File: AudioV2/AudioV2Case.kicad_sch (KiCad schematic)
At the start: 0 parts

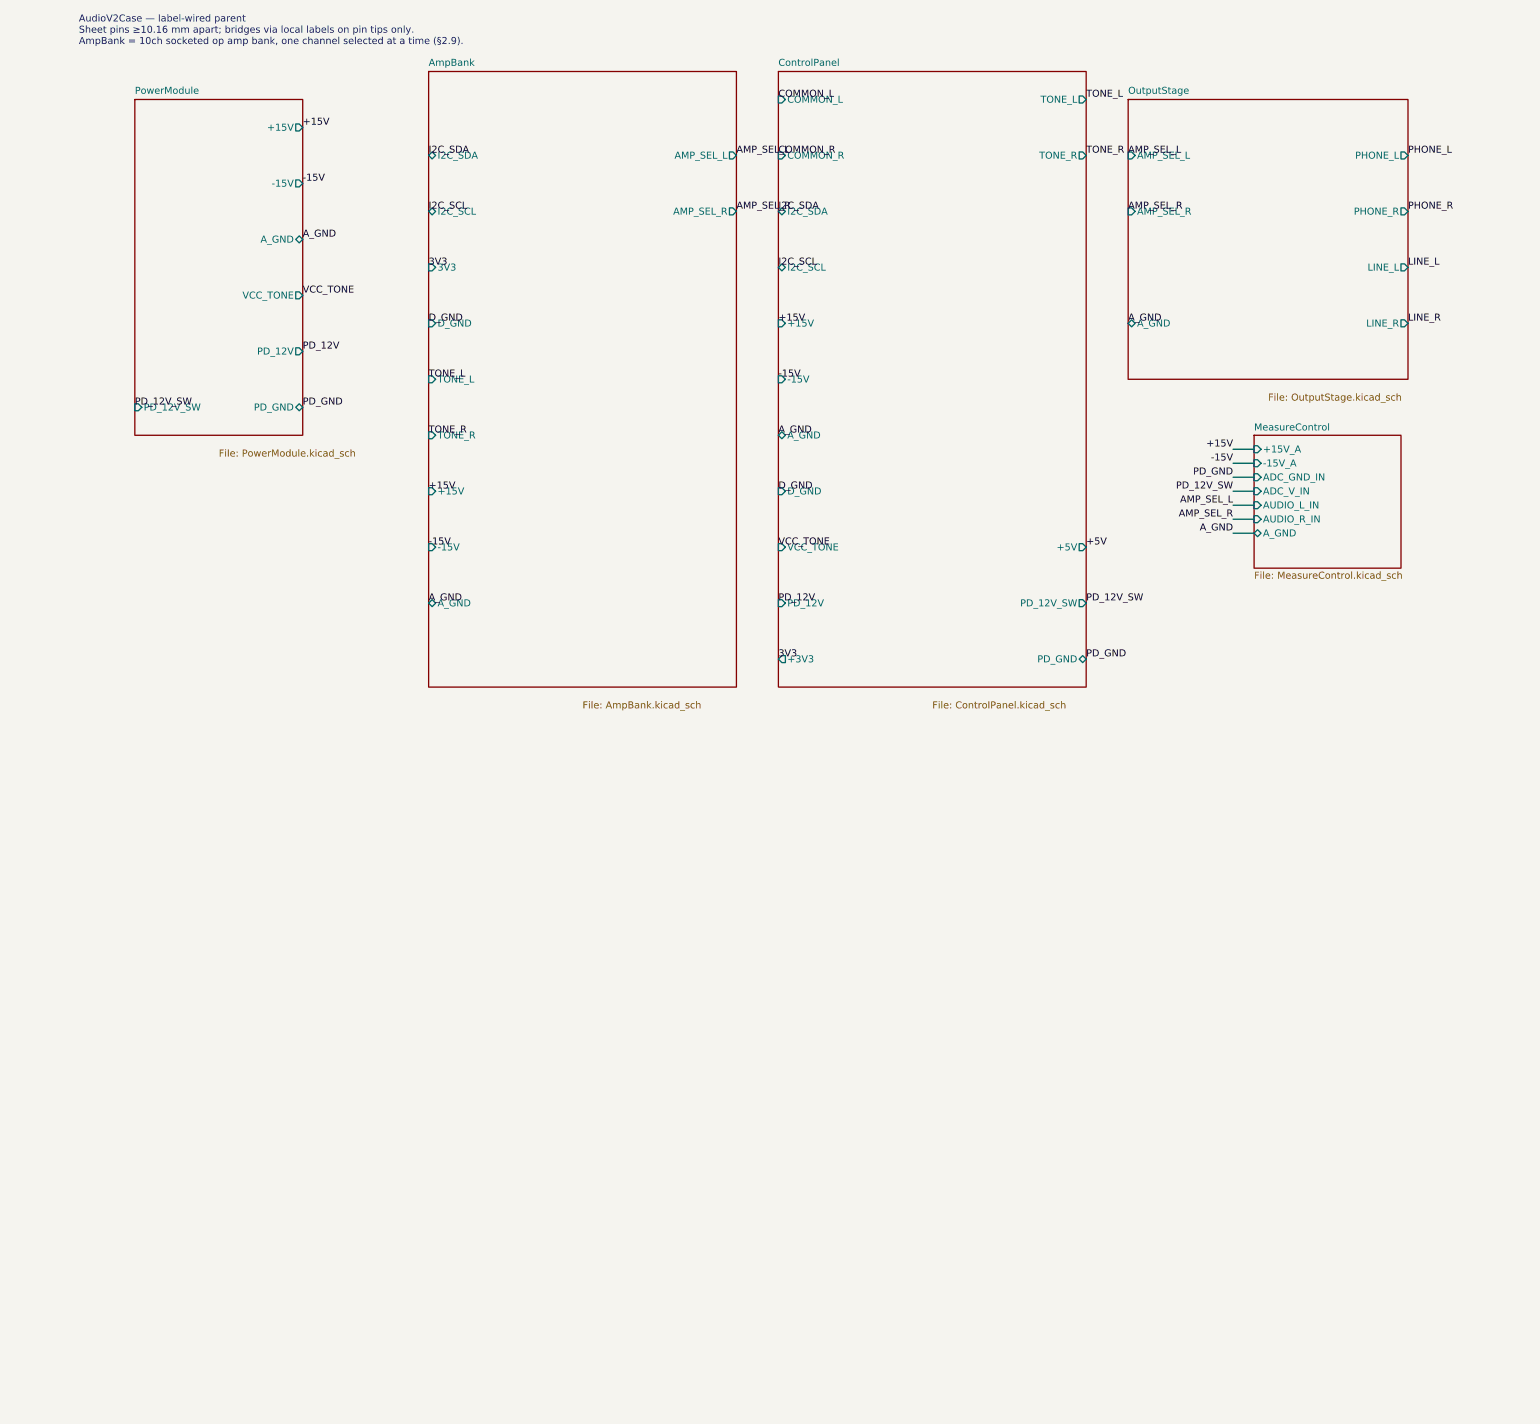
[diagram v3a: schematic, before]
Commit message: AudioV2: 母板 v0 を生成コードで組み立て、PowerModule と OutputStage を統合
確定している部分だけの骨格。PT2314 の移設と ControlPanel の解体は未決なので
触っていない（未決のまま足すと検証できない）。娘基板スロットは次のステップ。

    母板 v0 = PowerModule の全要素 ＋ OutputStage の全要素（+111.76mm 平行移動）

旧シートは sch_import で **KiCad が書いた S式のまま** 読むので、
**手描きの配線 92 本とジャンクション 33 個がそのまま母板へ移った**。
書き起こし直していたら失われていた部分。

統合の処理:
- 重複する階層ラベル A_GND（両シートが親経由で繋がっていた）を1本に。
  OutputStage 側はローカルラベルへ落として結線を保つ
- 各シンボルの instances パスを母板のシート UUID へ付け替え
- lib_symbols を名前で重複排除して統合
- 親から PowerModule / OutputStage のシートと、そのピン上にあった
  ラベル 14 個を外し、母板シート（階層ピン 13 本）＋ラベル 13 個に置換

新規ツール:
- build_motherboard.py — 母板の生成コード。再実行は冪等で、
  **UUID も決定的**（2回流してバイト一致を確認）。§2.8 の
  「再生成すると 348 行の uuid が毎回変わる」問題を持ち込まないため
- netlist_partition.py — ネットリストを「ピン集合の集合」で比較する。
  シート統合ではネット**名**は変わるが**分割**は変わってはいけない。
  sch_drift.py はワイヤを見ないので統合の検証には使えない

検証:
- ネットリストの分割が **310 ネットで完全一致**。名前だけ 4 件が
  /OutputStage/* → /MotherBoard/* に変化（シート内ネットなので当然）
- **ERC 60 件で前後同一**（内訳も同じ）
- sch_import --roundtrip が全シートでバイト一致

途中で 1 件やらかして直した: 平行移動量を 110.0mm にしたら配線の端点が
グリッドから外れ、endpoint_off_grid が 46 件出た。2.54 の倍数（111.76）に
してゼロへ。移動量はグリッドに乗せること、とコードにも注記した。

統合済みの旧2枚は AudioV2/legacy/ へ凍結（親からは参照されていない）。
編集しても設計には反映されない旨を legacy/README.md に明記。
wire_circuit_design.py の power / output も書き込み対象から外した。

Co-Authored-By: Claude Opus 5 <noreply@anthropic.com>
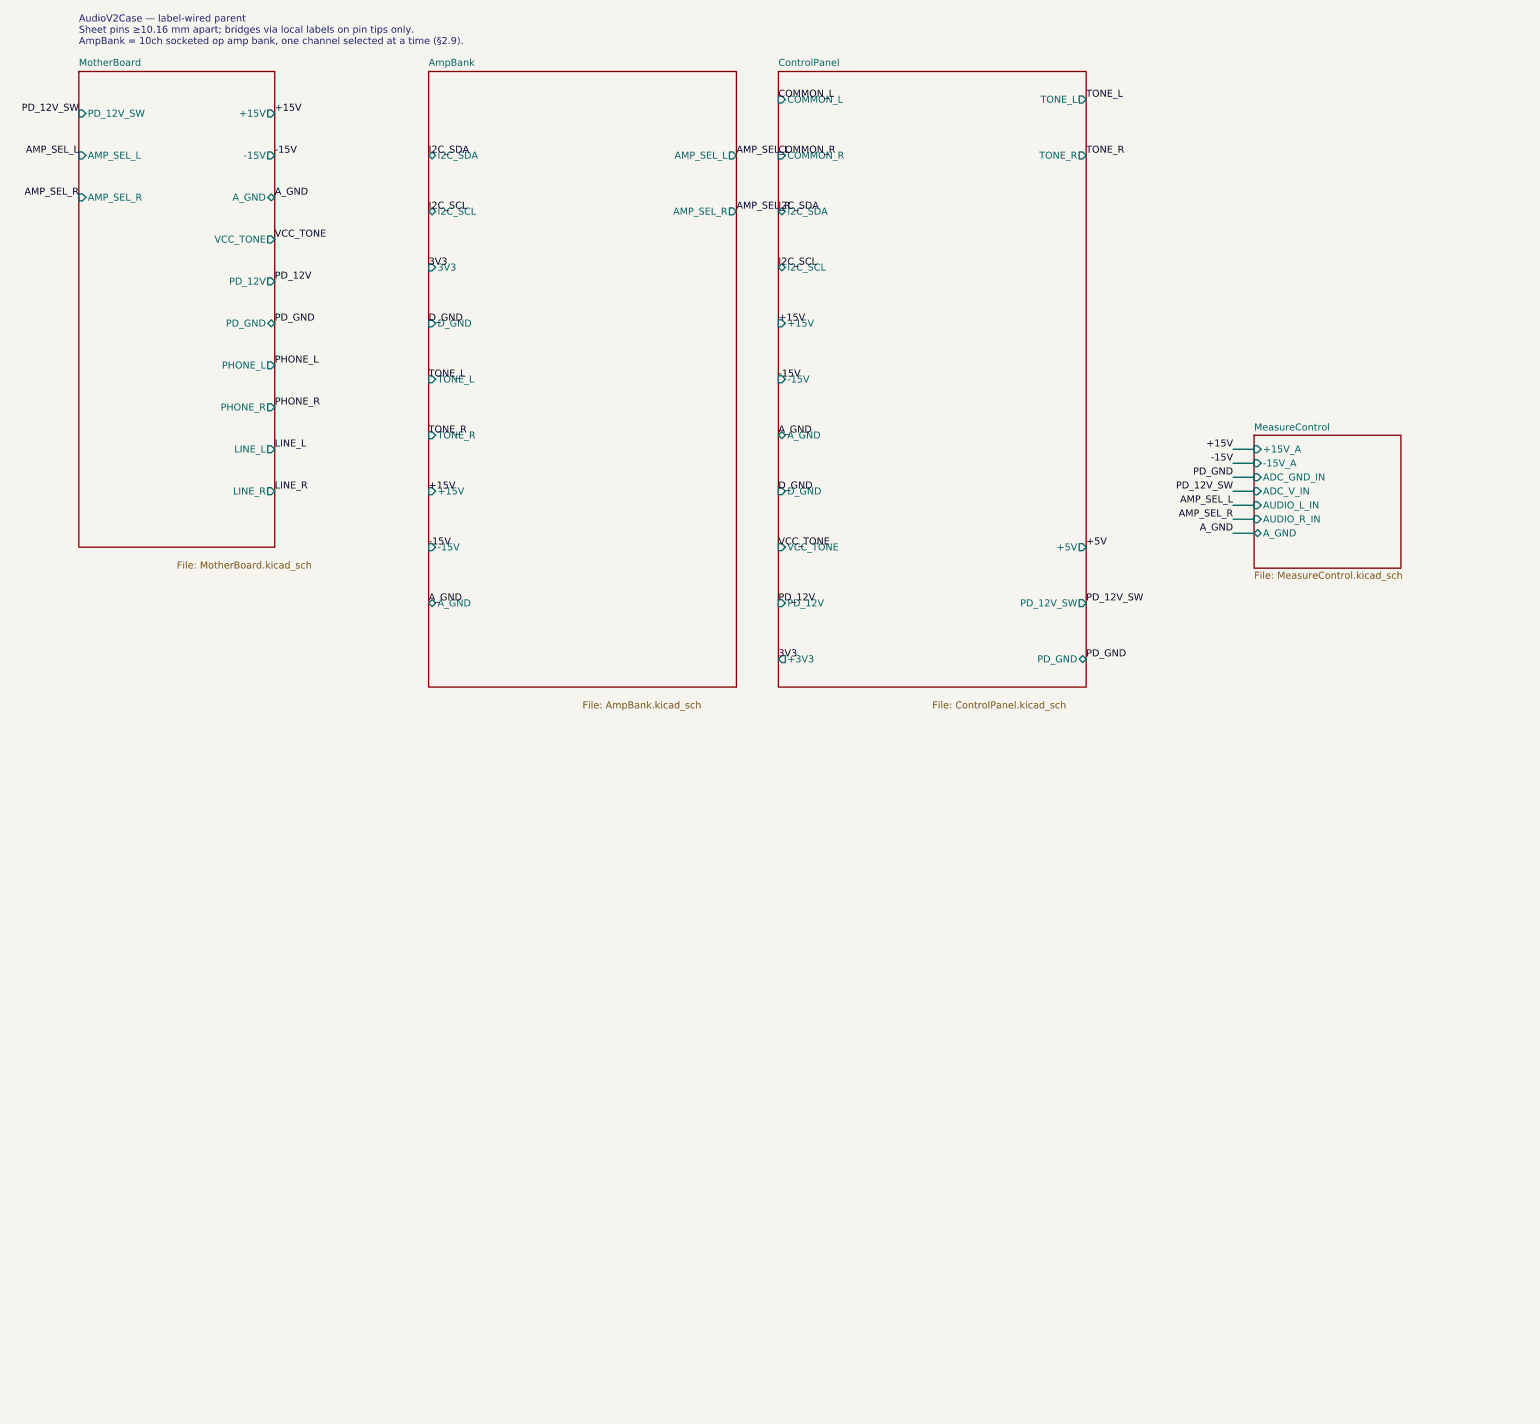
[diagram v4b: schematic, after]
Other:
- removed sheet OutputStage
- removed sheet PowerModule
- added sheet MotherBoard (MotherBoard.kicad_sch)

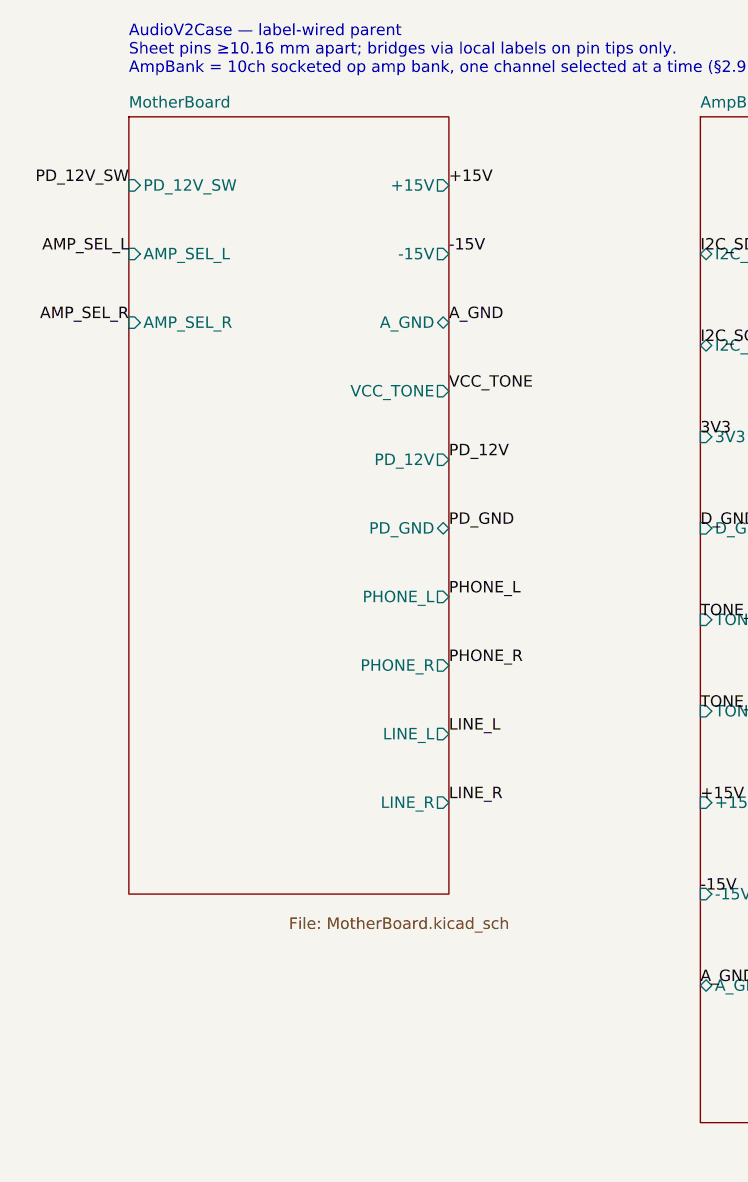
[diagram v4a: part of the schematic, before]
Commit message: AudioV2: 娘基板スロット2組を母板へ（D18 のピン割当を実装）
母板に J_ANA101/102（2x5）と J_PWR101/102（2x6）を置き、D18 のピン割当どおりに
ネットを配った。ピン座標は KiCad のシンボルから直接読む（_lib_pin_tips）ので
手で写す間違いが入らない。

D18 の抽象を母板側の具体へ落とすときに決まったこと:
- +5V_COIL の実体は ControlPanel の BP5293-50 が出す +5V。同日足された
  +5V(output) 階層ピンの行き先がこれで埋まった
- GND_COIL は独立ネットにして NT101（Device:NetTie_2）で D_GND へ1点結合。
  80mA級のコイルパルスを I2C の GND に流さないため。A6 で位置を見直す前提の暫定
- 番地は母板の配線で固定（D21）。slot1 = ADDR0/1 -> D_GND/D_GND = 0x20、
  slot2 = 3V3/D_GND = 0x21
- 母板の階層ピンは 13 -> 20 本（TONE_L/R・I2C_SDA/SCL・D_GND・3V3・+5V が増）

検証:
- ネットリストの分割が、足した5部品のピンを除くと **310 ネットで完全一致**。
  新規ネットはちょうど1本（/MotherBoard/GND_COIL）で、足した部品だけで閉じている
- **ERC 60 -> 56 件**。スロットが +5V を消費するようになり isolated_pin_label が4件消えた
- 部品 397 個すべてユニーク（重複0）
- 再実行が MotherBoard / AudioV2Case ともバイト一致

netlist_partition.py に --added を追加。足した参照のピンを後のネットリストから
取り除いてから比べるので「既存の分割は一切変わっていない」を機械的に言える。

途中で2件やらかして直した:
1. embed_lib_symbols() が 1 タブで `(symbol` を出すのに統合側の正規表現が
   2 タブ前提で、**新シンボルが lib_symbols から落ちていた**。落ちると KiCad が
   ピンを解決できず、**コネクタの全10ピンが1本のネットに潰れる**。
   netlist_partition が Net-(J_ANA101-Pad??) として検出した
2. daughter_slots() で sch_helpers.new_uid しか差し替えておらず、
   scaffold.uid を使う階層ラベル7本ぶん uuid 14 行が再実行で毎回変わっていた

Co-Authored-By: Claude Opus 5 <noreply@anthropic.com>
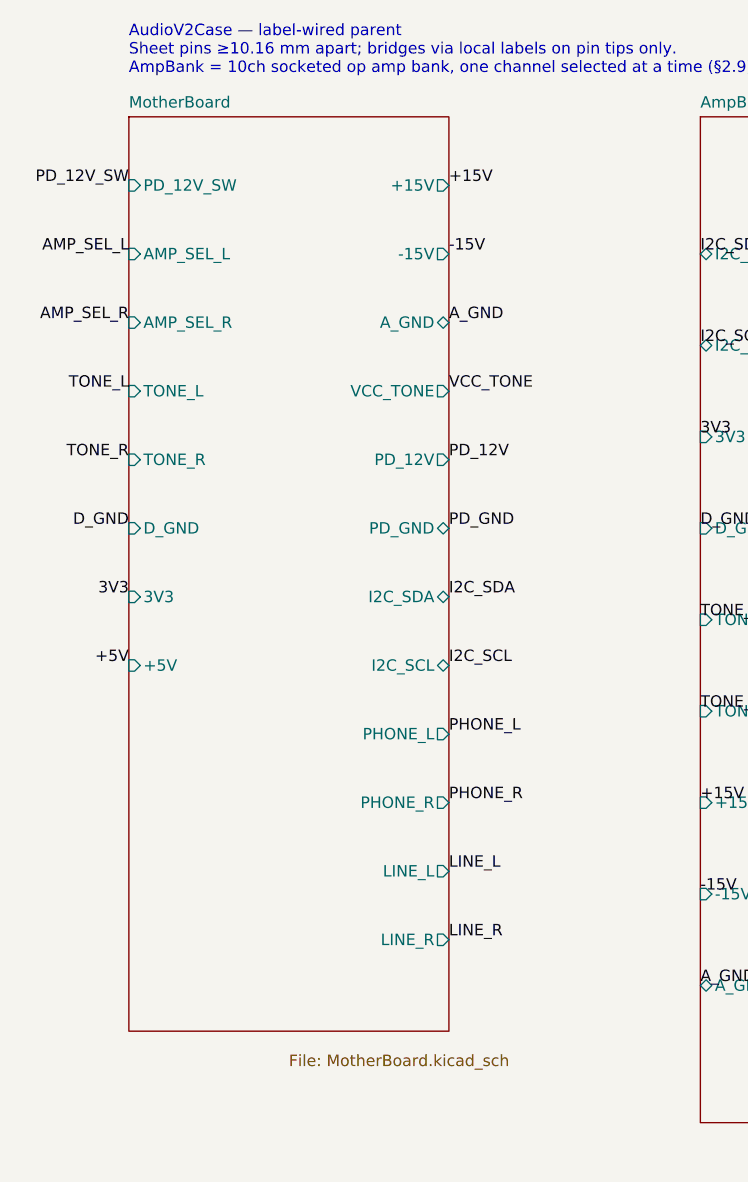
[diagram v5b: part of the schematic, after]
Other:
- sheet MotherBoard ports: added +5V, 3V3, D_GND, I2C_SCL, I2C_SDA, TONE_L, TONE_R; removed none
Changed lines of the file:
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@@
 	(sheet
 		(at 25.4 25.4)
-		(size 35.56 86.36)
+		(size 35.56 101.6)
 		(exclude_from_sim no)
 		(in_bom yes)
@@
 		)
 		(property "Sheetfile" "MotherBoard.kicad_sch"
-			(at 43.18 114.3 0)
+			(at 43.18 129.54 0)
 			(show_name no)
 			(do_not_autoplace no)
@@
 		)
 		(pin "AMP_SEL_R" input
-			(at 25.4 48.26 180)
+			(at 25.4 48.260000000000005 180)
+			(effects
+				(font
+					(size 1.27 1.27)
+				)
+				(justify left)
+			)
+		)
+		(pin "TONE_L" input
+			(at 25.4 55.88 180)
+			(effects
+				(font
+					(size 1.27 1.27)
+				)
+				(justify left)
+			)
+		)
+		(pin "TONE_R" input
+			(at 25.4 63.5 180)
+			(effects
+				(font
+					(size 1.27 1.27)
+				)
+				(justify left)
+			)
+		)
+		(pin "D_GND" input
+			(at 25.4 71.12 180)
+			(effects
+				(font
+					(size 1.27 1.27)
+				)
+				(justify left)
+			)
+		)
+		(pin "3V3" input
+			(at 25.4 78.74000000000001 180)
+			(effects
+				(font
+					(size 1.27 1.27)
+				)
+				(justify left)
+			)
+		)
+		(pin "+5V" input
+			(at 25.4 86.36000000000001 180)
 			(effects
 				(font
@@
 		)
 		(pin "A_GND" bidirectional
-			(at 60.96 48.26 0)
+			(at 60.96 48.260000000000005 0)
 			(effects
 				(font
@@
 			)
 		)
+		(pin "I2C_SDA" bidirectional
+			(at 60.96 78.74000000000001 0)
+			(effects
+				(font
+					(size 1.27 1.27)
+				)
+				(justify right)
+			)
+		)
+		(pin "I2C_SCL" bidirectional
+			(at 60.96 86.36000000000001 0)
+			(effects
+				(font
+					(size 1.27 1.27)
+				)
+				(justify right)
+			)
+		)
 		(pin "PHONE_L" output
-			(at 60.96 78.74 0)
+			(at 60.96 93.98 0)
 			(effects
 				(font
@@
 		)
 		(pin "PHONE_R" output
-			(at 60.96 86.36 0)
+			(at 60.96 101.6 0)
 			(effects
 				(font
@@
 		)
 		(pin "LINE_L" output
-			(at 60.96 93.98 0)
+			(at 60.96 109.22 0)
 			(effects
 				(font
@@
 		)
 		(pin "LINE_R" output
-			(at 60.96 101.6 0)
+			(at 60.96 116.84 0)
 			(effects
 				(font
@@
 	)
 	(label "AMP_SEL_R"
-		(at 25.4 48.26 180)
+		(at 25.4 48.260000000000005 180)
+		(effects
+			(font
+				(size 1.27 1.27)
+			)
+			(justify right bottom)
+		)
+	)
+	(label "TONE_L"
+		(at 25.4 55.88 180)
+		(effects
+			(font
+				(size 1.27 1.27)
+			)
+			(justify right bottom)
+		)
+	)
+	(label "TONE_R"
+		(at 25.4 63.5 180)
+		(effects
+			(font
+				(size 1.27 1.27)
+			)
+			(justify right bottom)
+		)
+	)
+	(label "D_GND"
+		(at 25.4 71.12 180)
+		(effects
+			(font
+				(size 1.27 1.27)
+			)
+			(justify right bottom)
+		)
+	)
+	(label "3V3"
+		(at 25.4 78.74000000000001 180)
+		(effects
+			(font
+				(size 1.27 1.27)
+			)
+			(justify right bottom)
+		)
+	)
+	(label "+5V"
+		(at 25.4 86.36000000000001 180)
 		(effects
 			(font
@@
 	)
 	(label "A_GND"
-		(at 60.96 48.26 0)
+		(at 60.96 48.260000000000005 0)
 		(effects
 			(font
@@
 		)
 	)
+	(label "I2C_SDA"
+		(at 60.96 78.74000000000001 0)
+		(effects
+			(font
+				(size 1.27 1.27)
+			)
+			(justify left bottom)
+		)
+	)
+	(label "I2C_SCL"
+		(at 60.96 86.36000000000001 0)
+		(effects
+			(font
+				(size 1.27 1.27)
+			)
+			(justify left bottom)
+		)
+	)
 	(label "PHONE_L"
-		(at 60.96 78.74 0)
+		(at 60.96 93.98 0)
 		(effects
 			(font
@@
 	)
 	(label "PHONE_R"
-		(at 60.96 86.36 0)
+		(at 60.96 101.6 0)
 		(effects
 			(font
@@
 	)
 	(label "LINE_L"
-		(at 60.96 93.98 0)
+		(at 60.96 109.22 0)
 		(effects
 			(font
@@
 	)
 	(label "LINE_R"
-		(at 60.96 101.6 0)
-		(effects
-			(font
+		(at 60.96 116.84 0)
+		(effects
+			(font
